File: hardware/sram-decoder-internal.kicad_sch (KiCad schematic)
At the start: 1 part, among them U13 74LVC138A

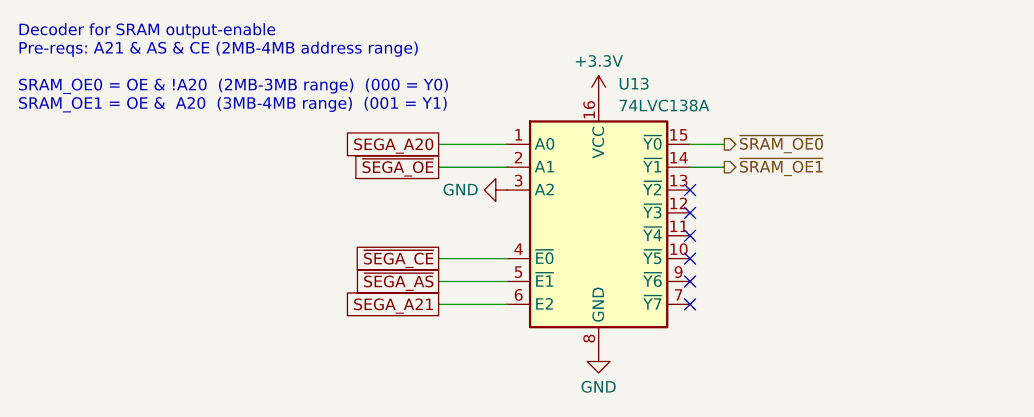
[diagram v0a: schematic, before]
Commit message: Reannotate schematics and drop debug bridges
Parts are now numbered starting at 0 for cart, 100 for SRAM, 300 for
microcontroller.

Also, drop debug bridges that made routing more difficult and had the
same names across prototype boards.

Hopefully this will help avoid naming conflicts for the unified PCB.

Also, redo prototype PCB layouts.

Now that all the names have changed, update board layouts.
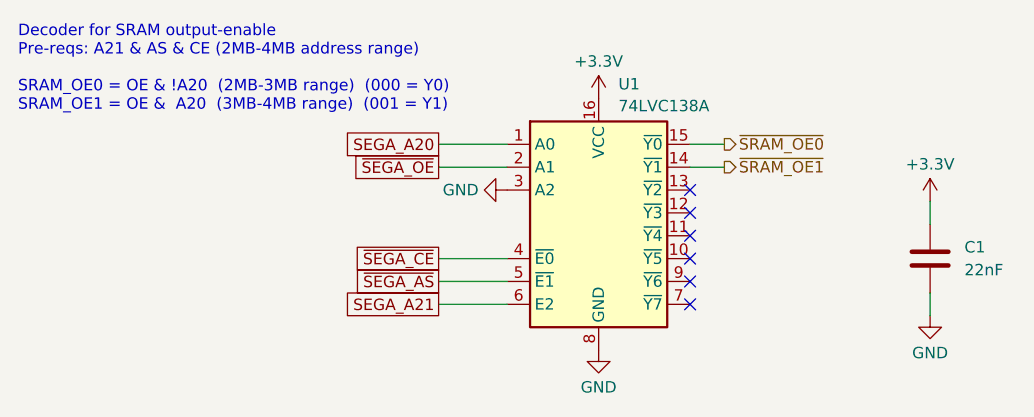
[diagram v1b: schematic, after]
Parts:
- added C1: 22nF, Capacitor_SMD:C_0603_1608Metric, symbol Device:C
- renumbered U13 to U1
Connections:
- net +3.3V: now also C1.1
- net GND: now also C1.2

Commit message: Drop A18 GND connection
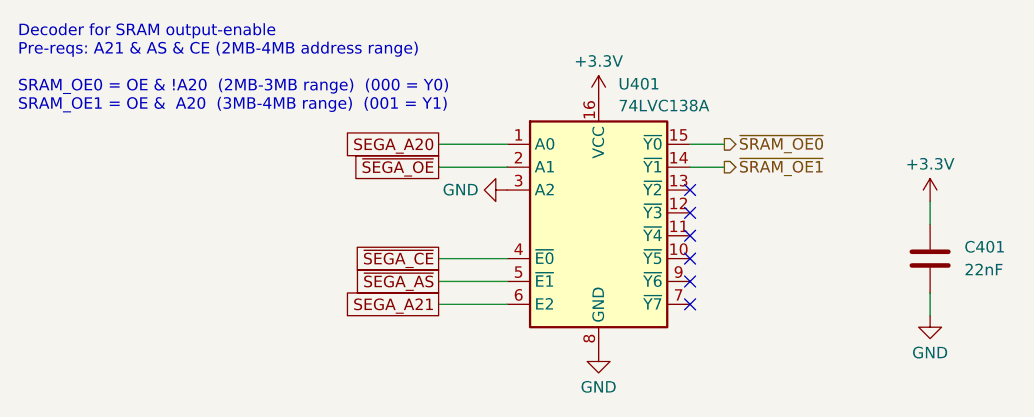
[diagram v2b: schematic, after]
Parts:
- renumbered C1 to C401, U1 to U401
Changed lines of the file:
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@@
 		(dnp no)
 		(fields_autoplaced yes)
-		(property "Reference" "#PWR016"
+		(property "Reference" "#PWR0403"
 			(at 83.82 63.5 0)
 			(effects
@@
 		(dnp no)
 		(fields_autoplaced yes)
-		(property "Reference" "#PWR014"
+		(property "Reference" "#PWR0401"
 			(at 67.31 39.37 0)
 			(effects
@@
 		(dnp no)
 		(fields_autoplaced yes)
-		(property "Reference" "#PWR018"
+		(property "Reference" "#PWR0405"
 			(at 120.65 59.69 0)
 			(effects
@@
 		(dnp no)
 		(fields_autoplaced yes)
-		(property "Reference" "#PWR017"
+		(property "Reference" "#PWR0404"
 			(at 120.65 44.45 0)
 			(effects
@@
 		(dnp no)
 		(fields_autoplaced yes)
-		(property "Reference" "#PWR015"
+		(property "Reference" "#PWR0402"
 			(at 83.82 33.02 0)
 			(effects
@@
 		(dnp no)
 		(fields_autoplaced yes)
-		(property "Reference" "C1"
+		(property "Reference" "C401"
 			(at 124.46 45.7199 0)
 			(effects
@@
 		(dnp no)
 		(fields_autoplaced yes)
-		(property "Reference" "U1"
+		(property "Reference" "U401"
 			(at 86.0141 27.6055 0)
 			(effects
